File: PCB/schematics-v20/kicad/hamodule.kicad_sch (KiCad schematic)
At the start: 92 parts, among them J1 Conn_01x02_Male, J10 USB_C_Receptacle_USB2.0, J11 2604-1104, J12 2604-1104, J13 EspSense, J2 2604-1102, J3 GND|5V, J4 USB | PS, J5 GND|3.3V, J6 Conn_01x02_Male, J7 Current Jumper, J8 Conn_01x02_Male, J9 EspRelays, K1 AQG12205, K2 AQG12205, K3 AQG12205, K4 AQG12205, Q1 SS8050-SMD, Q2 SS8050, SW1 Switch, SW2 Switch, U1 LD1117AV33, U2 ESP32-WROOM-32E, U4 CP2102N-A01-GQFN28, U5 ULN2003A, U6 LDA210-PDIP, U7 LDA210-PDIP, U8 SHT4x

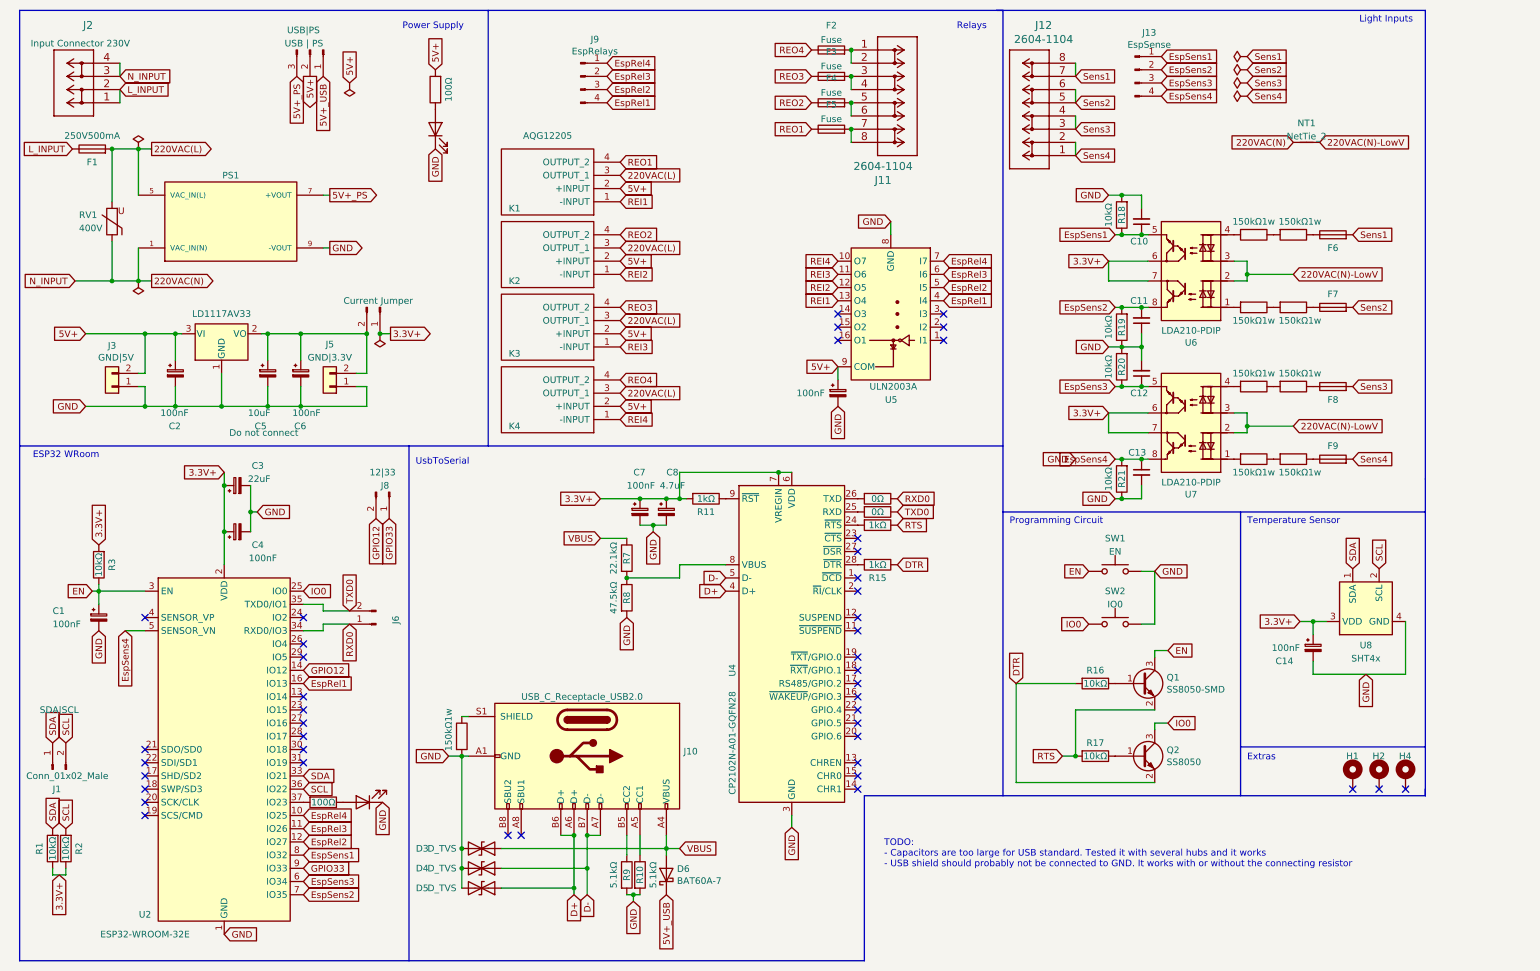
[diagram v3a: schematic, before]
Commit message: adding caps, SSRelays
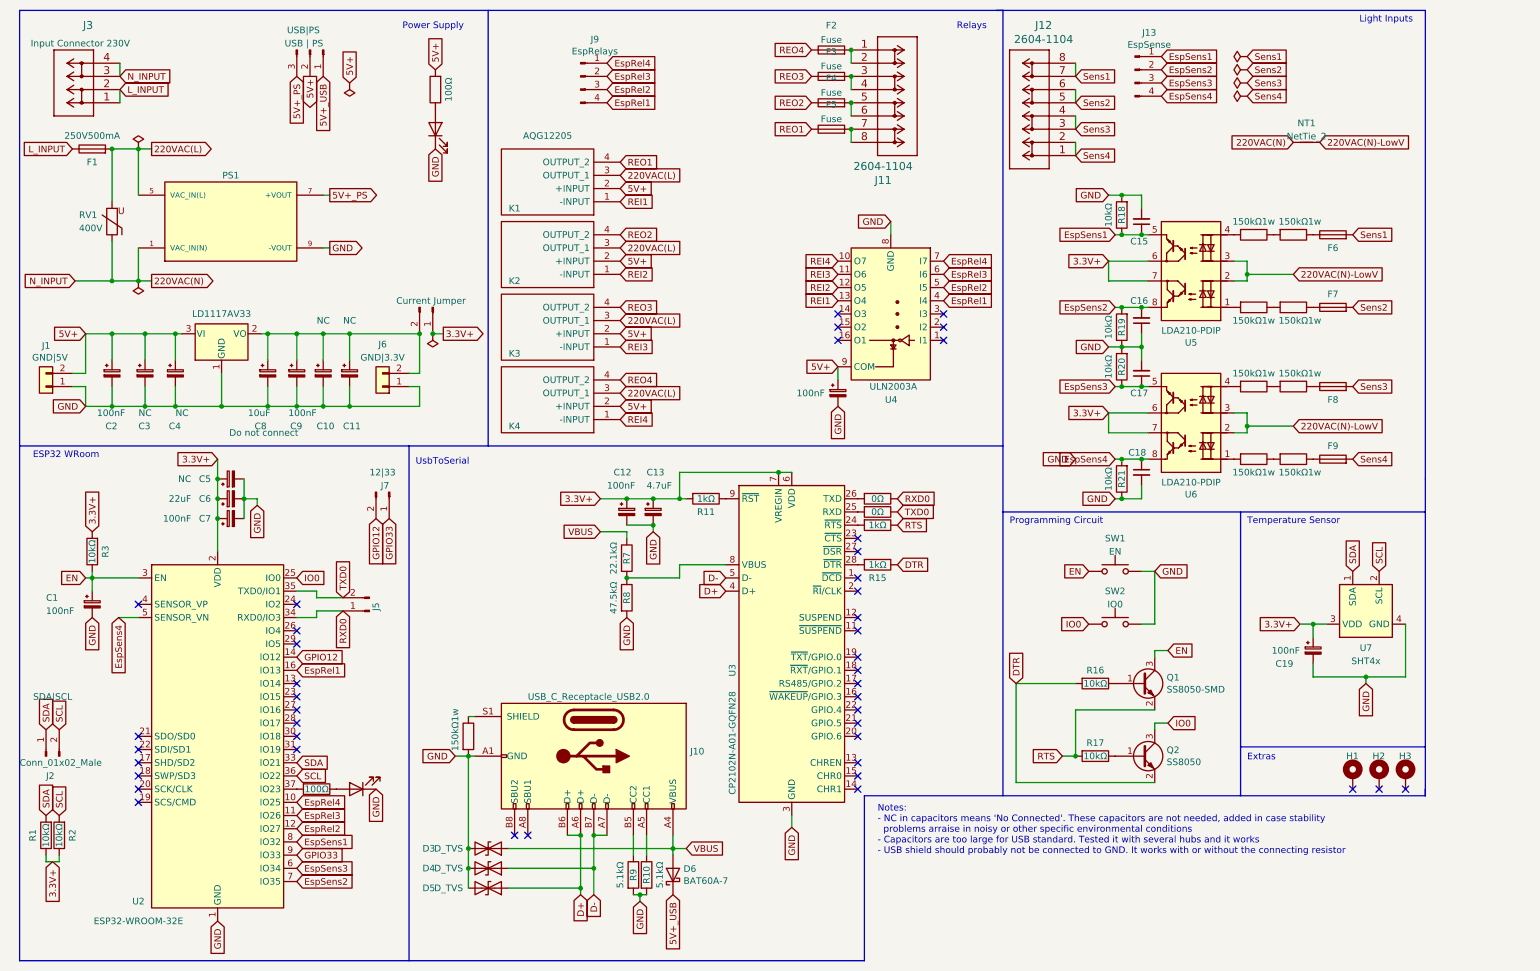
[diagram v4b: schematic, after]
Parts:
- added C10, C11, C3: NC, Capacitor_SMD:C_0603_1608Metric_Pad1.08x0.95mm_HandSolder, symbol Device:C_Polarized_Small
- added C2: 100nF, Capacitor_SMD:C_0603_1608Metric_Pad1.08x0.95mm_HandSolder, symbol Device:C_Polarized_Small
- added C6: 22uF, Capacitor_SMD:C_0603_1608Metric_Pad1.08x0.95mm_HandSolder, symbol Device:C_Polarized_Small
- C4: renamed from C2; value 100nF -> NC
- C5: renamed from C3; value 22uF -> NC
- renumbered C7 to C12, C8 to C13, C9 to C14, C10 to C15, C11 to C16, C12 to C17, C13 to C18, C14 to C19, C4 to C7, C5 to C8, C6 to C9, H4 to H3, J3 to J1, J1 to J2, J2 to J3, J6 to J5, J5 to J6, J8 to J7, J7 to J8, U4 to U3, U5 to U4, U6 to U5, U7 to U6, U8 to U7
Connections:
- net 3.3V+: now also C6.1
- net 5V+: now also C2.1, C3.1
- net GND: now also C10.2, C11.2, C2.2, C3.2, C6.2
- net at C8.1, C9.1, J6.2 (Pin_2)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: now also C10.1, C11.1
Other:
- note added: "Notes: - NC in capacitors means 'No Connected'. These capacitors are not needed, added in case stability problems arraise in noisy or other specific environmental conditions - Capacitors are too large for USB standard. Tested it with several hubs and it works - USB shield should probably not be connected to GND. It works with or without the connecting resistor"
- note removed: "TODO: - Capacitors are too large for USB standard. Tested it with several hubs and it works - USB shield should probably not be connected to GND. It works with or without the connecting resistor"
- moved on the sheet: C1, C12, C13, C19, C5, C7, C9, D3, D4, D5, D6, J1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
